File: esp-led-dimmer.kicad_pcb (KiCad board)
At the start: 2 copper layers, 22.5 x 36.5 mm, 16 parts, among them J1 Barrel Jack 3A, J2 ESP-01, J3 LED 1, J4 LED 2, Q1 AO3400A, Q2 AO3400A, U1 TPS5430DDA

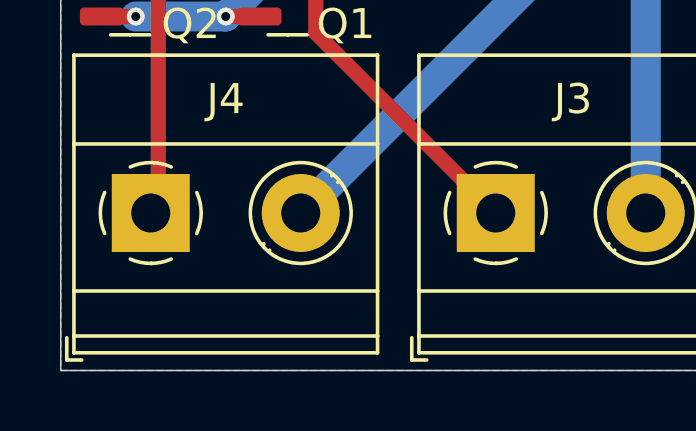
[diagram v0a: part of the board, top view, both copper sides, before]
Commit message: Add JLCPCB component IDs for PCBA
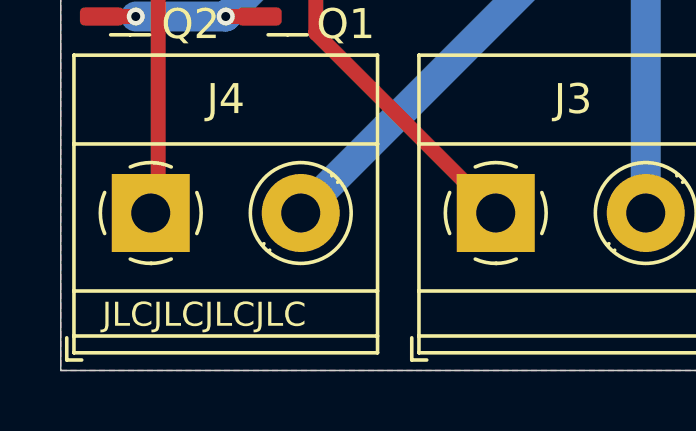
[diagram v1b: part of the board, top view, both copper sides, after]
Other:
- board text added: "JLCJLCJLCJLC"
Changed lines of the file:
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@@
 			)
 		)
+		(property "LCSC" "C1779"
+			(at 0 0 0)
+			(layer "F.SilkS")
+			(hide yes)
+			(effects
+				(font
+					(size 1.27 1.27)
+					(thickness 0.15)
+				)
+			)
+		)
 		(property ki_fp_filters "C_*")
 		(sheetname "Root")
@@
 		(tags "capacitor")
 		(property "Reference" "C3"
-			(at 0 -1.85 360)
+			(at 0 -1.85 0)
 			(layer "F.SilkS")
 			(effects
@@
 		)
 		(property "Value" "100µF"
-			(at 0 1.85 360)
+			(at 0 1.85 0)
 			(layer "F.Fab")
 			(effects
@@
 			)
 		)
+		(property "LCSC" "C15008"
+			(at 0 0 0)
+			(layer "F.SilkS")
+			(hide yes)
+			(effects
+				(font
+					(size 1.27 1.27)
+					(thickness 0.15)
+				)
+			)
+		)
 		(property ki_fp_filters "C_*")
 		(sheetname "Root")
@@
 		)
 		(fp_text user "${REFERENCE}"
-			(at 0 0 360)
+			(at 0 0 0)
 			(layer "F.Fab")
 			(effects
@@
 			)
 		)
+		(property "LCSC" "C25744"
+			(at 0 0 0)
+			(layer "F.SilkS")
+			(hide yes)
+			(effects
+				(font
+					(size 1.27 1.27)
+					(thickness 0.15)
+				)
+			)
+		)
 		(property ki_fp_filters "R_*")
 		(sheetname "Root")
@@
 			)
 		)
+		(property "LCSC" "C159006"
+			(at 0 0 0)
+			(layer "F.SilkS")
+			(hide yes)
+			(effects
+				(font
+					(size 1.27 1.27)
+					(thickness 0.15)
+				)
+			)
+		)
 		(property ki_fp_filters "R_*")
 		(sheetname "Root")
@@
 			)
 		)
+		(property "LCSC" "C2935984"
+			(at 0 0 0)
+			(layer "F.SilkS")
+			(hide yes)
+			(effects
+				(font
+					(size 1.27 1.27)
+					(thickness 0.15)
+				)
+			)
+		)
 		(property ki_fp_filters "Connector*:*_1x??_*")
 		(sheetname "Root")
@@
 			)
 		)
+		(property "LCSC" "C720558"
+			(at 0 0 0)
+			(layer "F.SilkS")
+			(hide yes)
+			(effects
+				(font
+					(size 1.27 1.27)
+					(thickness 0.15)
+				)
+			)
+		)
 		(property ki_fp_filters "BarrelJack*")
 		(sheetname "Root")
@@
 			)
 		)
+		(property "LCSC" "C15195"
+			(at 0 0 0)
+			(layer "F.SilkS")
+			(hide yes)
+			(effects
+				(font
+					(size 1.27 1.27)
+					(thickness 0.15)
+				)
+			)
+		)
 		(property ki_fp_filters "C_*")
 		(sheetname "Root")
@@
 		(tags "SOT TO_SOT_SMD")
 		(property "Reference" "Q2"
-			(at 2.015834 1.206004 360)
+			(at 2.015834 1.206004 0)
 			(layer "F.SilkS")
 			(effects
@@
 		)
 		(property "Value" "AO3400A"
-			(at 0 2.4 360)
+			(at 0 2.4 0)
 			(layer "F.Fab")
 			(effects
@@
 		)
 		(property "Footprint" "Package_TO_SOT_SMD:SOT-23"
-			(at 0 0 360)
+			(at 0 0 0)
 			(layer "F.Fab")
 			(hide yes)
@@
 		)
 		(property "Datasheet" "http://www.aosmd.com/pdfs/datasheet/AO3400A.pdf"
-			(at 0 0 360)
+			(at 0 0 0)
 			(layer "F.Fab")
 			(hide yes)
@@
 		)
 		(property "Description" "30V Vds, 5.7A Id, N-Channel MOSFET, SOT-23"
-			(at 0 0 360)
+			(at 0 0 0)
 			(layer "F.Fab")
 			(hide yes)
@@
 		)
 		(fp_text user "${REFERENCE}"
-			(at 0 0 360)
+			(at 0 0 0)
 			(layer "F.Fab")
 			(effects
@@
 			)
 		)
+		(property "LCSC" "C5188434"
+			(at 0 0 0)
+			(layer "F.SilkS")
+			(hide yes)
+			(effects
+				(font
+					(size 1.27 1.27)
+					(thickness 0.15)
+				)
+			)
+		)
 		(property ki_fp_filters "TerminalBlock*:*")
 		(sheetname "Root")
@@
 			)
 		)
+		(property "LCSC" "C9864"
+			(at 0 0 0)
+			(layer "F.SilkS")
+			(hide yes)
+			(effects
+				(font
+					(size 1.27 1.27)
+					(thickness 0.15)
+				)
+			)
+		)
 		(property ki_fp_filters "TI*SO*PowerPAD*ThermalVias*")
 		(sheetname "Root")
@@
 		(tags "SOD-323")
 		(property "Reference" "D1"
-			(at -2.75 0 360)
+			(at -2.75 0 0)
 			(layer "F.SilkS")
 			(effects
@@
 		)
 		(property "Value" "1N5819"
-			(at 0.1 1.9 360)
+			(at 0.1 1.9 0)
 			(layer "F.Fab")
 			(effects
@@
 			)
 		)
+		(property "LCSC" "C191023"
+			(at 0 0 0)
+			(layer "F.SilkS")
+			(hide yes)
+			(effects
+				(font
+					(size 1.27 1.27)
+					(thickness 0.15)
+				)
+			)
+		)
 		(property ki_fp_filters "D*DO?41*")
 		(sheetname "Root")
@@
 		)
 		(fp_text user "${REFERENCE}"
-			(at 0 -1.85 360)
+			(at 0 -1.85 0)
 			(layer "F.Fab")
 			(effects
@@
 			)
 		)
+		(property "LCSC" "C20917"
+			(at 0 0 0)
+			(layer "F.SilkS")
+			(hide yes)
+			(effects
+				(font
+					(size 1.27 1.27)
+					(thickness 0.15)
+				)
+			)
+		)
 		(property ki_fp_filters "SOT?23*")
 		(sheetname "Root")
@@
 			)
 		)
+		(property "LCSC" "C5289430"
+			(at 0 0 0)
+			(layer "F.SilkS")
+			(hide yes)
+			(effects
+				(font
+					(size 1.27 1.27)
+					(thickness 0.15)
+				)
+			)
+		)
 		(property ki_fp_filters "Choke_* *Coil* Inductor_* L_*")
 		(sheetname "Root")
@@
 		)
 		(fp_text user "${REFERENCE}"
-			(at 0 0 360)
+			(at 0 0 0)
 			(layer "F.Fab")
 			(effects
@@
 		)
 	)
+	(gr_text "JLCJLCJLCJLC"
+		(at 140.3 117.9 0)
+		(layer "F.SilkS")
+		(effects
+			(font
+				(size 0.8 0.8)
+				(thickness 0.1)
+			)
+			(justify left bottom)
+		)
+	)
